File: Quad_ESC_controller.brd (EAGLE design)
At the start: 23.1 x 34 mm, 23 parts, among them Y1 ECS-80-S-4X

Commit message: Library Changes for Backplane :)
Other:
- board size 23.1 x 34 mm -> 22.9 x 34 mm
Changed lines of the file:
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@@
 <setting verticaltext="up"/>
 </settings>
-<grid distance="10" unitdist="mil" unit="mil" style="lines" multiple="1" display="no" altdistance="5" altunitdist="mil" altunit="mil"/>
+<grid distance="10" unitdist="mil" unit="mil" style="lines" multiple="1" display="no" altdistance="1" altunitdist="mil" altunit="mil"/>
 <layers>
 <layer number="1" name="Top" color="4" fill="1" visible="yes" active="yes"/>
@@
 <plain>
 <wire x1="0" y1="0" x2="22.86" y2="0" width="0" layer="20"/>
-<wire x1="22.86" y1="0" x2="23.114" y2="34.036" width="0" layer="20"/>
-<wire x1="23.114" y1="34.036" x2="0" y2="34.036" width="0" layer="20"/>
+<wire x1="22.86" y1="0" x2="22.86" y2="34.036" width="0" layer="20"/>
+<wire x1="22.86" y1="34.036" x2="0" y2="34.036" width="0" layer="20"/>
 <wire x1="0" y1="34.036" x2="0" y2="0" width="0" layer="20"/>
 </plain>
@@
 <contactref element="U$2" pad="P$1"/>
 <contactref element="R4" pad="1"/>
-<wire x1="17.298" y1="21.7036" x2="20.32" y2="21.7036" width="0.6096" layer="1"/>
-<wire x1="20.32" y1="21.7036" x2="20.32" y2="19.7036" width="0.6096" layer="1"/>
-<wire x1="20.32" y1="19.7036" x2="17.298" y2="19.7036" width="0.6096" layer="1"/>
-<wire x1="17.298" y1="19.7036" x2="17.298" y2="21.7036" width="0.6096" layer="1"/>
+<wire x1="17.298" y1="21.5766" x2="20.32" y2="21.5766" width="0.6096" layer="1"/>
+<wire x1="20.32" y1="21.5766" x2="20.32" y2="19.5766" width="0.6096" layer="1"/>
+<wire x1="20.32" y1="19.5766" x2="17.298" y2="19.5766" width="0.6096" layer="1"/>
+<wire x1="17.298" y1="19.5766" x2="17.298" y2="21.5766" width="0.6096" layer="1"/>
 <wire x1="10.892" y1="17.47758125" x2="10.892" y2="18.246" width="0.6096" layer="1"/>
 <wire x1="10.892" y1="18.246" x2="10.934" y2="18.288" width="0.6096" layer="1"/>
@@
 <wire x1="7.62" y1="7.874" x2="8.914" y2="6.58" width="0.6096" layer="1"/>
 <wire x1="8.914" y1="6.58" x2="8.914" y2="5.576" width="0.6096" layer="1"/>
-<wire x1="20.32" y1="21.7036" x2="20.32" y2="28.702" width="0.6096" layer="1"/>
+<wire x1="20.32" y1="21.5766" x2="20.32" y2="28.702" width="0.6096" layer="1"/>
 <wire x1="4.953" y1="16.852" x2="4.064" y2="17.741" width="0.6096" layer="16"/>
 <wire x1="4.064" y1="17.741" x2="4.064" y2="18.542" width="0.6096" layer="16"/>
@@
 <wire x1="11.188" y1="18.542" x2="11.938" y2="18.542" width="0.6096" layer="1"/>
 <wire x1="11.938" y1="18.542" x2="13.0996" y2="19.7036" width="0.6096" layer="1"/>
-<wire x1="13.0996" y1="19.7036" x2="17.298" y2="19.7036" width="0.6096" layer="1"/>
+<wire x1="13.0996" y1="19.7036" x2="17.298" y2="19.5766" width="0.6096" layer="1"/>
 </signal>
 <signal name="CAN_TX">
@@
 <wire x1="10.6398" y1="6.1242" x2="11.2042" y2="6.1242" width="0.254" layer="1"/>
 <wire x1="11.2042" y1="6.1242" x2="11.43" y2="6.35" width="0.254" layer="1"/>
-<wire x1="11.43" y1="6.35" x2="11.43" y2="7.366" width="0.254" layer="1"/>
-<wire x1="11.43" y1="7.366" x2="11.684" y2="7.62" width="0.254" layer="1"/>
-<wire x1="16.51" y1="7.62" x2="16.764" y2="7.366" width="0.254" layer="1"/>
-<wire x1="16.764" y1="7.366" x2="16.764" y2="6.604" width="0.254" layer="1"/>
-<wire x1="16.764" y1="6.604" x2="16.51" y2="6.35" width="0.254" layer="1"/>
-<wire x1="11.684" y1="7.62" x2="16.51" y2="7.62" width="0.254" layer="1"/>
+<wire x1="11.43" y1="6.35" x2="11.43" y2="7.3152" width="0.254" layer="1"/>
+<wire x1="11.43" y1="7.3152" x2="11.7348" y2="7.62" width="0.254" layer="1"/>
+<wire x1="16.51" y1="7.62" x2="16.7386" y2="7.3914" width="0.254" layer="1"/>
+<wire x1="16.7386" y1="7.3914" x2="16.7386" y2="6.5786" width="0.254" layer="1"/>
+<wire x1="16.7386" y1="6.5786" x2="16.51" y2="6.35" width="0.254" layer="1"/>
+<wire x1="11.7348" y1="7.62" x2="16.51" y2="7.62" width="0.254" layer="1"/>
 <wire x1="16.51" y1="6.35" x2="14.478" y2="6.35" width="0.254" layer="1"/>
 </signal>
@@
 <wire x1="15.748" y1="2.54" x2="14.478" y2="2.54" width="0.254" layer="1"/>
 <wire x1="15.415" y1="5.667" x2="16.002" y2="5.08" width="0.254" layer="16"/>
-<wire x1="8.534" y1="9.788" x2="8.534" y2="7.85803125" width="0.254" layer="1"/>
-<wire x1="9.652" y1="6.74003125" x2="9.652" y2="5.842" width="0.254" layer="1"/>
+<wire x1="8.534" y1="9.788" x2="8.534" y2="7.93423125" width="0.254" layer="1"/>
+<wire x1="9.652" y1="6.81623125" x2="9.652" y2="5.842" width="0.254" layer="1"/>
 <wire x1="9.652" y1="5.842" x2="9.827" y2="5.667" width="0.254" layer="1"/>
 <wire x1="9.827" y1="5.667" x2="13.072" y2="5.667" width="0.254" layer="1"/>
-<wire x1="8.534" y1="7.85803125" x2="9.652" y2="6.74003125" width="0.254" layer="1"/>
+<wire x1="8.534" y1="7.93423125" x2="9.652" y2="6.81623125" width="0.254" layer="1"/>
 </signal>
 <signal name="TIM3_CH1">
@@
 <wire x1="18.288" y1="7.112" x2="19.304" y2="8.128" width="0.254" layer="1"/>
 <wire x1="19.304" y1="8.128" x2="22.098" y2="8.128" width="0.254" layer="1"/>
-<wire x1="22.098" y1="8.128" x2="22.352" y2="8.382" width="0.254" layer="1"/>
-<wire x1="22.352" y1="8.382" x2="22.352" y2="17.526" width="0.254" layer="1"/>
-<wire x1="22.352" y1="17.526" x2="22.1744" y2="17.7036" width="0.254" layer="1"/>
-<wire x1="22.1744" y1="17.7036" x2="20.32" y2="17.7036" width="0.254" layer="1"/>
+<wire x1="22.352" y1="8.382" x2="22.098" y2="8.128" width="0.254" layer="1"/>
+<wire x1="20.32" y1="17.5766" x2="22.0474" y2="17.5766" width="0.254" layer="1"/>
+<wire x1="22.0474" y1="17.5766" x2="22.352" y2="17.272" width="0.254" layer="1"/>
+<wire x1="22.352" y1="17.272" x2="22.352" y2="8.382" width="0.254" layer="1"/>
 </signal>
 <signal name="CAN_L">
@@
 <wire x1="17.8308" y1="4.8768" x2="17.8308" y2="7.30138125" width="0.254" layer="1"/>
 <wire x1="21.082" y1="16.51" x2="20.32" y2="15.748" width="0.254" layer="1"/>
-<wire x1="20.32" y1="15.748" x2="20.32" y2="15.7036" width="0.254" layer="1"/>
+<wire x1="20.32" y1="15.748" x2="20.32" y2="15.5766" width="0.254" layer="1"/>
 <wire x1="21.844" y1="8.89" x2="21.844" y2="16.256" width="0.254" layer="1"/>
 <wire x1="21.844" y1="16.256" x2="21.59" y2="16.51" width="0.254" layer="1"/>
@@
 <wire x1="21.336" y1="10.668" x2="21.336" y2="13.462" width="0.254" layer="1"/>
 <wire x1="21.336" y1="13.462" x2="21.0944" y2="13.7036" width="0.254" layer="1"/>
-<wire x1="21.0944" y1="13.7036" x2="20.32" y2="13.7036" width="0.254" layer="1"/>
+<wire x1="21.0944" y1="13.7036" x2="20.32" y2="13.5766" width="0.254" layer="1"/>
 <wire x1="17.69578125" y1="8.1788" x2="19.67698125" y2="10.16" width="0.254" layer="1"/>
 <wire x1="13.5128" y1="14.4216" x2="11.176" y2="12.0848" width="0.254" layer="16"/>
@@
 <wire x1="11.4018" y1="11.4018" x2="11.176" y2="11.176" width="0.254" layer="16"/>
 <wire x1="15.24" y1="30.11058125" x2="17.7292" y2="27.62138125" width="0.254" layer="16"/>
-<wire x1="20.32" y1="11.7036" x2="17.2524" y2="8.636" width="0.254" layer="1"/>
+<wire x1="20.32" y1="11.5766" x2="17.2524" y2="8.636" width="0.254" layer="1"/>
 <wire x1="11.814" y1="8.636" x2="10.798" y2="9.652" width="0.254" layer="1"/>
 <wire x1="17.2524" y1="8.636" x2="11.814" y2="8.636" width="0.254" layer="1"/>
@@
 <contactref element="RESET" pad="2"/>
 <contactref element="U$4" pad="NRST"/>
-<wire x1="21.2215875" y1="18.7534" x2="21.2641875" y2="18.796" width="0.254" layer="1"/>
-<wire x1="21.2641875" y1="18.796" x2="21.336" y2="18.796" width="0.254" layer="1"/>
-<wire x1="17.298" y1="17.7036" x2="18.3478" y2="18.7534" width="0.254" layer="1"/>
-<wire x1="18.3478" y1="18.7534" x2="21.2215875" y2="18.7534" width="0.254" layer="1"/>
-<wire x1="21.336" y1="18.796" x2="21.59" y2="19.05" width="0.254" layer="1"/>
+<wire x1="17.298" y1="17.5766" x2="18.211846875" y2="18.601" width="0.254" layer="1"/>
+<wire x1="18.211846875" y1="18.601" x2="21.0691875" y2="18.601" width="0.254" layer="1"/>
+<wire x1="21.0691875" y1="18.601" x2="21.59" y2="19.1218125" width="0.254" layer="1"/>
 <wire x1="2.54" y1="26.41" x2="3.39" y2="25.56" width="0.254" layer="1"/>
 <wire x1="3.39" y1="25.56" x2="3.39" y2="23.876" width="0.254" layer="1"/>
@@
 <wire x1="18.7706" y1="32.7914" x2="9.1694" y2="32.7914" width="0.254" layer="1"/>
 <wire x1="9.1694" y1="32.7914" x2="7.62" y2="31.242" width="0.254" layer="1"/>
-<wire x1="21.59" y1="19.05" x2="21.59" y2="29.972" width="0.254" layer="1"/>
+<wire x1="21.59" y1="19.1218125" x2="21.59" y2="29.972" width="0.254" layer="1"/>
 <wire x1="21.59" y1="29.972" x2="18.7706" y2="32.7914" width="0.254" layer="1"/>
 </signal>
@@
 <contactref element="R1" pad="2"/>
 <contactref element="U$4" pad="PF1-OSC_OUT"/>
-<wire x1="10.414" y1="21.59" x2="9.398" y2="20.574" width="0.254" layer="16"/>
+<wire x1="9.906" y1="21.082" x2="9.398" y2="20.574" width="0.254" layer="16"/>
 <via x="9.398" y="20.574" extent="1-16" drill="0.35"/>
 <wire x1="9.398" y1="20.574" x2="9.398" y2="18.352" width="0.254" layer="1"/>
 <wire x1="9.398" y1="18.352" x2="9.334" y2="18.288" width="0.254" layer="1"/>
-<wire x1="9.906" y1="25.312" x2="10.414" y2="24.804" width="0.254" layer="16"/>
-<wire x1="10.414" y1="24.804" x2="10.414" y2="21.59" width="0.254" layer="16"/>
+<wire x1="9.906" y1="25.312" x2="9.906" y2="21.082" width="0.254" layer="16"/>
 </signal>
 <signal name="N$1">
@@
 <mfgpreviewcolor name="substratecolor" color="0xFF786E46"/>
 </mfgpreviewcolors>
-<errors>
-</errors>
 </board>
 </drawing>

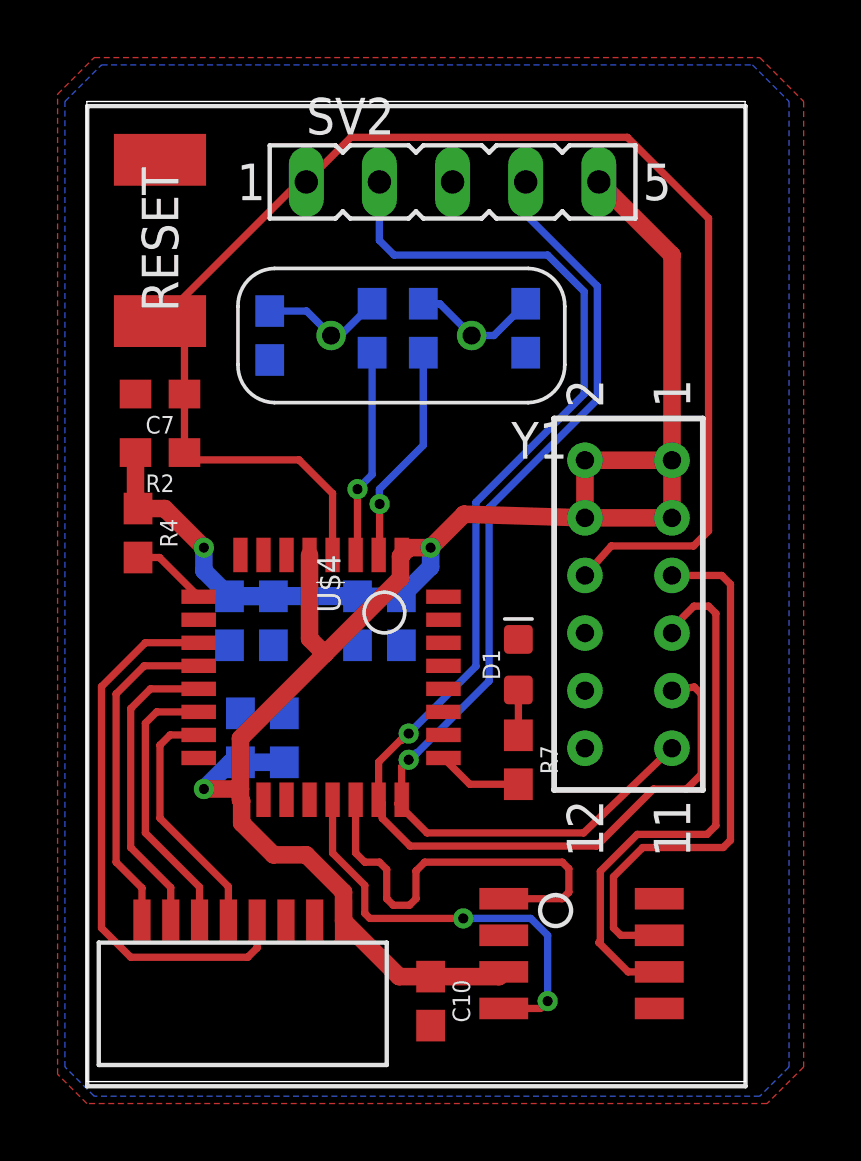
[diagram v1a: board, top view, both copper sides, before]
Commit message: Routing Update
rerouted new connector into board :)
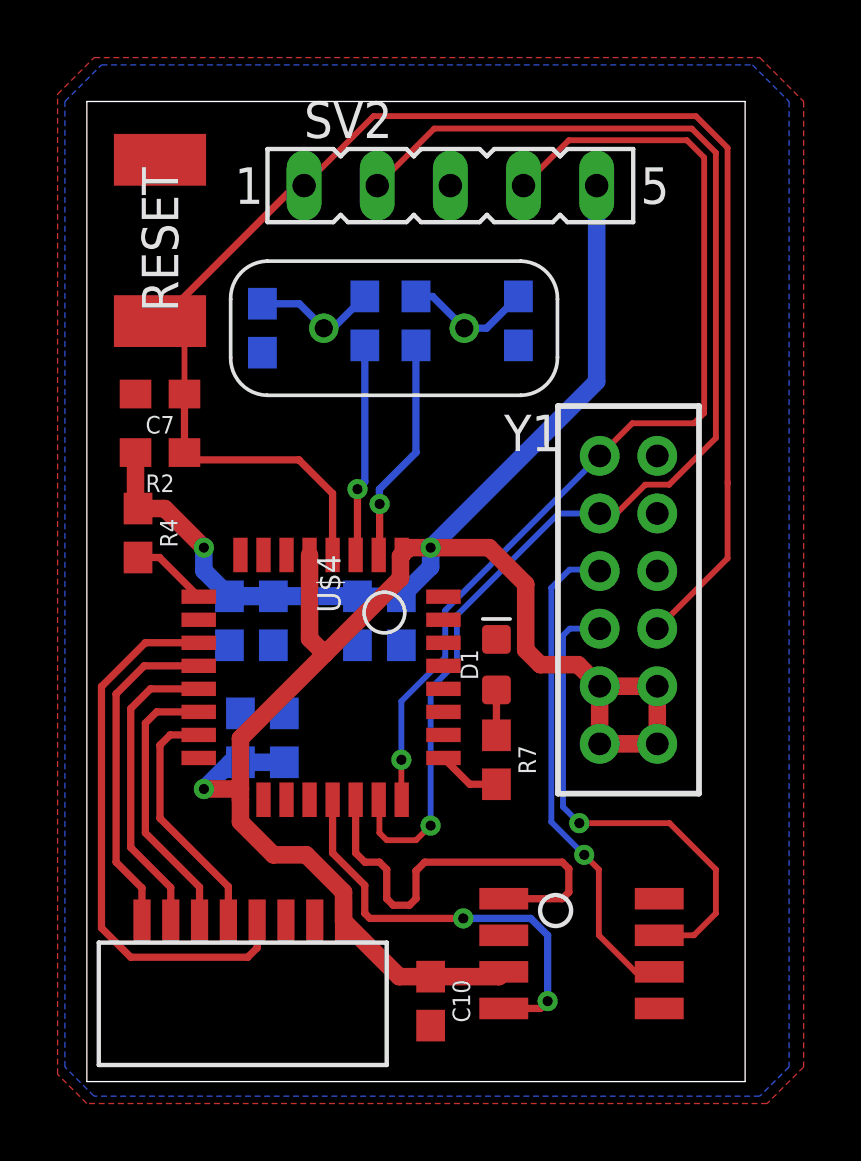
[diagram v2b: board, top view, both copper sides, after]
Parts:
- U$3: value BACKPLANE_CONNECTORS -> BACKPLANE_CONNECTORSBKP; device BLHeli_32 45A:BACKPLANE_CONNECTORS -> BLHeli_32 45A:BACKPLANE_CONNECTORS_BKP
- moved D1 0.76 mm to (14.2, 14.5)
- moved R7 0.76 mm to (14.2, 11.2)
- moved R1 0.36 mm to (9.65, 26.4)
- moved C8 0.36 mm to (15.0, 26.4)
- moved R3 0.36 mm to (11.4, 26.4)
- moved Y1 0.36 mm to (10.7, 26.2)
- moved C9 0.36 mm to (6.10, 26.2)
- moved SV2 0.15 mm to (12.6, 31.1)
- moved U$3 0.13 mm to (18.8, 16.7)
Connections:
- net +3V3: now also U$3.1, U$3.2, U$3.3, U$3.4; no longer U$3.25, U$3.26, U$3.27, U$3.28
- net CAN_H: now also U$3.5; no longer U$3.29
- net CAN_L: now also U$3.7; no longer U$3.31
- net N$7: now also U$3.8; no longer U$3.32
- net N$8: now also U$3.12; no longer U$3.36
- net NRST: now also U$3.6; no longer U$3.30
- net SWCLK: now also U$3.11; no longer U$3.35
- net SWDIO: now also U$3.9; no longer U$3.33
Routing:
- net +3V3: track 80.4 -> 85.9 mm
- net SWDIO: track 47.6 -> 45.3 mm
- net NRST: track 51.5 -> 53.6 mm
- net CAN_L: track 19.2 -> 17.3 mm, vias 0 -> 1
- net CAN_H: track 19.1 -> 17.3 mm, vias 0 -> 1
- net SWCLK: track 36.7 -> 35.1 mm
- net LED: track 2.98 -> 2.22 mm
